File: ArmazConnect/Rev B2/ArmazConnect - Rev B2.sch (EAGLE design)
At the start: 38 parts, among them X0 NC3FAAV2, X1 NC3FAAV2, X2 NC3FAAV2, X3 NC3FAAV2, X4 NC5FAV-SW, X5 NC5MAV-SW, X6 NC5FAV-SW, X8 87832-26

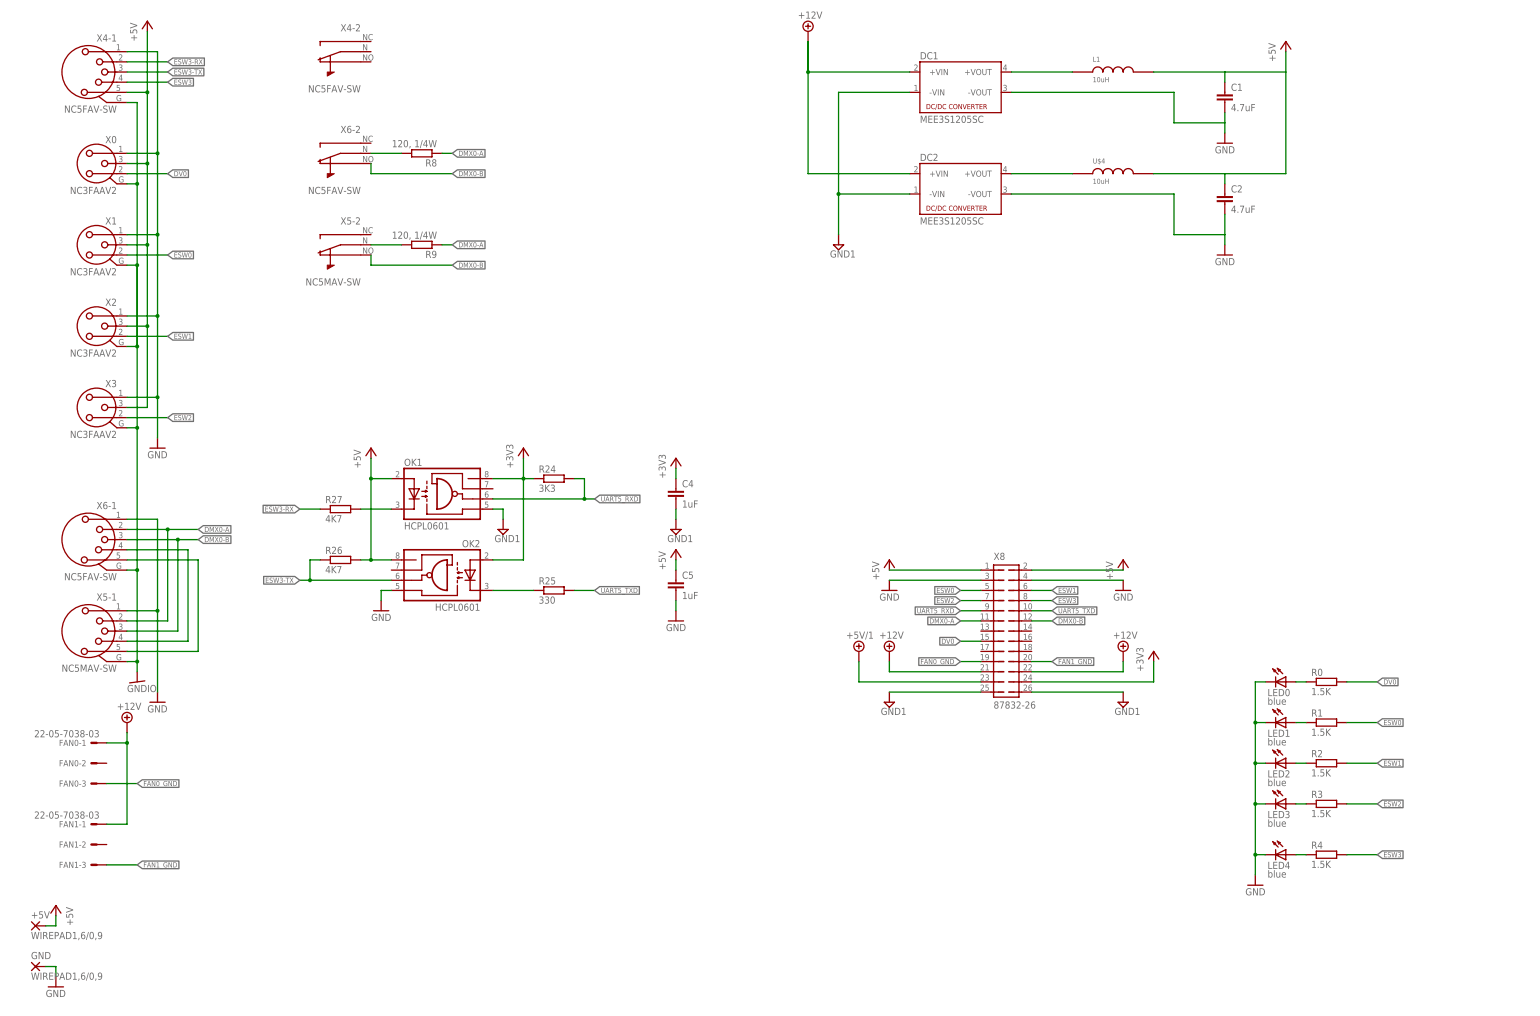
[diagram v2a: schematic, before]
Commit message: dc-dc-converter.lbr updated. Fiducials added. Silkscreen improved.
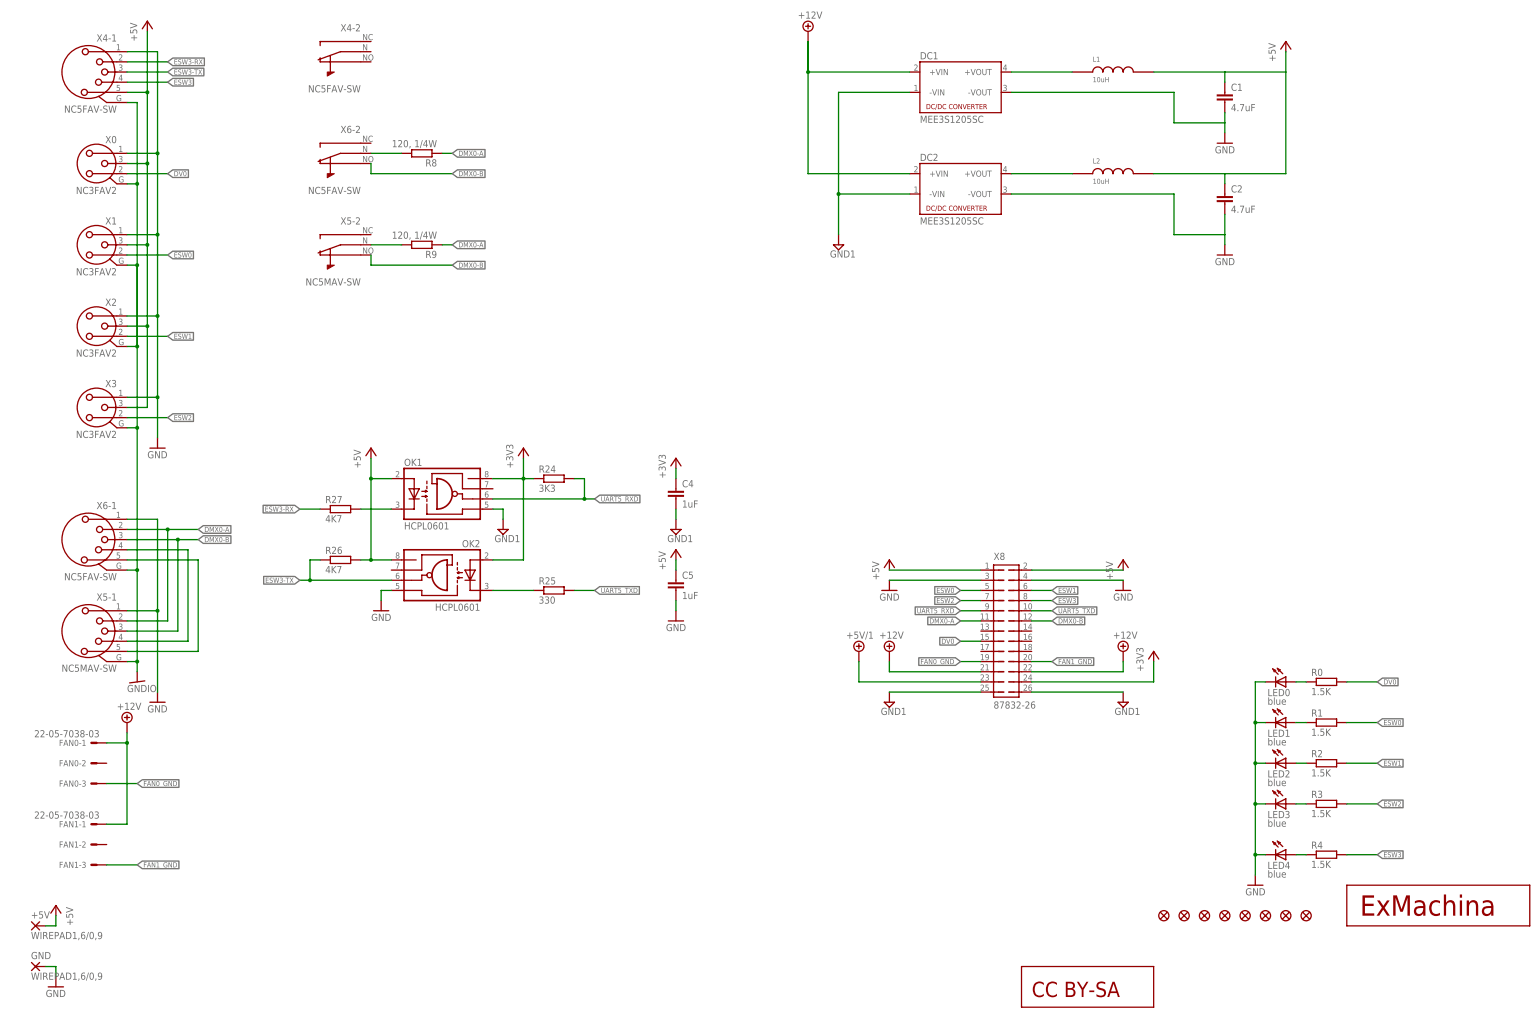
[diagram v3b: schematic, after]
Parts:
- added FI1, FI2, FI3, FI4, FI5, FI6, FI7, FI8: FIDUCIAL1X2, SparkFun:FIDUCIAL1X2
- added U$1: EXMACHINA-LOGO-NAME, exmachina:EXMACHINA-LOGO-NAME
- added U$2: CC-BY-SA, cc-by-sa:CC-BY-SA
- FAN0, FAN1: OC_FARNELL 9731610 -> (none)
- X0, X1, X2, X3: value NC3FAAV2 -> NC3FAV2; device con-neutrik_ag:NC3FAAV2 -> con-neutrik_ag:NC3FAV2; OC_FARNELL 1310038 -> (none)
- renumbered U$4 to L2
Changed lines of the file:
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@@
 </classes>
 <parts>
-<part name="X1" library="con-neutrik_ag" deviceset="NC3" device="FAAV2" value="NC3FAAV2">
-<attribute name="OC_FARNELL" value="1310038"/>
-</part>
-<part name="X2" library="con-neutrik_ag" deviceset="NC3" device="FAAV2" value="NC3FAAV2">
-<attribute name="OC_FARNELL" value="1310038"/>
-</part>
-<part name="X3" library="con-neutrik_ag" deviceset="NC3" device="FAAV2" value="NC3FAAV2">
-<attribute name="OC_FARNELL" value="1310038"/>
-</part>
+<part name="X1" library="con-neutrik_ag" deviceset="NC3" device="FAV2" value="NC3FAV2"/>
+<part name="X2" library="con-neutrik_ag" deviceset="NC3" device="FAV2" value="NC3FAV2"/>
+<part name="X3" library="con-neutrik_ag" deviceset="NC3" device="FAV2" value="NC3FAV2"/>
 <part name="X4" library="con-neutrik_ag" deviceset="NC5?-SW" device="FAV" value="NC5FAV-SW">
 <attribute name="OC_FARNELL" value="1310093"/>
@@
 </part>
 <part name="GND13" library="supply1" deviceset="GND" device=""/>
-<part name="X0" library="con-neutrik_ag" deviceset="NC3" device="FAAV2" value="NC3FAAV2">
-<attribute name="OC_FARNELL" value="1310038"/>
-</part>
+<part name="X0" library="con-neutrik_ag" deviceset="NC3" device="FAV2" value="NC3FAV2"/>
 <part name="R0" library="rcl" deviceset="R-EU_" device="R0603" value="1.5K">
 <attribute name="MF" value="MULTICOMP"/>
@@
 <attribute name="MF" value="MOLEX"/>
 <attribute name="MPN" value="22-05-7038"/>
-<attribute name="OC_FARNELL" value="9731610"/>
 </part>
 <part name="FAN1" library="con-molex" deviceset="22-?-03" device="05-7038">
 <attribute name="MF" value="MOLEX"/>
 <attribute name="MPN" value="22-05-7038"/>
-<attribute name="OC_FARNELL" value="9731610"/>
 </part>
 <part name="SUPPLY3" library="supply2" deviceset="+12V" device=""/>
@@
 <part name="SUPPLY5" library="supply2" deviceset="GND1" device=""/>
 <part name="L1" library="murata-inductance" deviceset="84103C" device="" value="10uH"/>
-<part name="U$4" library="murata-inductance" deviceset="84103C" device="" value="10uH"/>
+<part name="L2" library="murata-inductance" deviceset="84103C" device="" value="10uH"/>
 <part name="C1" library="rcl" deviceset="C-EU" device="C0603" value="4.7uF"/>
 <part name="C2" library="rcl" deviceset="C-EU" device="C0603" value="4.7uF"/>
 <part name="GND4" library="supply1" deviceset="GND" device=""/>
+<part name="FI1" library="SparkFun" deviceset="FIDUCIAL" device="1X2"/>
+<part name="FI2" library="SparkFun" deviceset="FIDUCIAL" device="1X2"/>
+<part name="FI3" library="SparkFun" deviceset="FIDUCIAL" device="1X2"/>
+<part name="FI4" library="SparkFun" deviceset="FIDUCIAL" device="1X2"/>
+<part name="FI5" library="SparkFun" deviceset="FIDUCIAL" device="1X2"/>
+<part name="FI6" library="SparkFun" deviceset="FIDUCIAL" device="1X2"/>
+<part name="FI7" library="SparkFun" deviceset="FIDUCIAL" device="1X2"/>
+<part name="FI8" library="SparkFun" deviceset="FIDUCIAL" device="1X2"/>
+<part name="U$1" library="exmachina" deviceset="EXMACHINA-LOGO" device="-NAME"/>
+<part name="U$2" library="cc-by-sa" deviceset="CC-BY-SA" device=""/>
 </parts>
 <sheets>
@@
 <instance part="SUPPLY5" gate="G$1" x="208.28" y="195.58"/>
 <instance part="L1" gate="L$1" x="276.86" y="238.76"/>
-<instance part="U$4" gate="L$1" x="276.86" y="213.36"/>
+<instance part="L2" gate="L$1" x="276.86" y="213.36"/>
 <instance part="C1" gate="G$1" x="304.8" y="233.68"/>
 <instance part="C2" gate="G$1" x="304.8" y="208.28"/>
 <instance part="GND4" gate="1" x="304.8" y="220.98" rot="MR0"/>
+<instance part="FI1" gate="G$1" x="289.56" y="27.94"/>
+<instance part="FI2" gate="G$1" x="294.64" y="27.94"/>
+<instance part="FI3" gate="G$1" x="299.72" y="27.94"/>
+<instance part="FI4" gate="G$1" x="304.8" y="27.94"/>
+<instance part="FI5" gate="G$1" x="309.88" y="27.94"/>
+<instance part="FI6" gate="G$1" x="314.96" y="27.94"/>
+<instance part="FI7" gate="G$1" x="320.04" y="27.94"/>
+<instance part="FI8" gate="G$1" x="325.12" y="27.94"/>
+<instance part="U$1" gate="G$1" x="358.14" y="30.48"/>
+<instance part="U$2" gate="A" x="269.24" y="10.16"/>
 </instances>
 <busses>
@@
 <wire x1="287.02" y1="238.76" x2="304.8" y2="238.76" width="0.1524" layer="91"/>
 <pinref part="P+4" gate="1" pin="+5V"/>
-<pinref part="U$4" gate="L$1" pin="2"/>
+<pinref part="L2" gate="L$1" pin="2"/>
 <wire x1="304.8" y1="238.76" x2="320.04" y2="238.76" width="0.1524" layer="91"/>
 <wire x1="320.04" y1="238.76" x2="320.04" y2="243.84" width="0.1524" layer="91"/>
@@
 <net name="N$7" class="0">
 <segment>
-<pinref part="U$4" gate="L$1" pin="1"/>
+<pinref part="L2" gate="L$1" pin="1"/>
 <pinref part="DC2" gate="G$1" pin="+VOUT"/>
 <wire x1="266.7" y1="213.36" x2="251.46" y2="213.36" width="0.1524" layer="91"/>

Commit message: Added GERBER RS274X files for Varmo - Rev A1
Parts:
- C1, C2: MF (none) -> MULTICOMP; MPN (none) -> MC0603X475K6R3CT; OC_FARNELL (none) -> 2320811
- DC1, DC2: MF (none) -> MURATA POWER SOLUTIONS; MPN (none) -> MEE3S1205SC; OC_FARNELL (none) -> 2083742
- FAN0, FAN1: OC_FARNELL (none) -> 9731610
- FI1, FI2, FI3, FI4, FI5, FI6, FI7, FI8, U$1, U$2: OC_FARNELL (none) -> unknown
- L1, L2: MF (none) -> WURTH ELEKTRONIK; MPN (none) -> 744045100; OC_FARNELL (none) -> 1800409
- R25: MPN MCMR04X3300FTL -> MCMR06X3300FTL; OC_FARNELL 2072927 -> 2073472
- R8, R9: MPN MCHP05W4F1200T5E -> MCMR06X1200FTL; OC_FARNELL 1576447 -> 2073369
- X0, X1, X2, X3: MPN (none) -> NC3FAAV2; OC_FARNELL (none) -> 1310038
